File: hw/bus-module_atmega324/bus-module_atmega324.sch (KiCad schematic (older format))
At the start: 35 parts, among them J1 CONN_10X2, J2 CONN_10X2, J3 CONN-ISP-6, J5 CONN_1, J6 CONN_1, J7 CONN_1, J8 CONN_1, U1 ATMEGA324-TQFP44, U2 7,3728MHz, U3 25LCXXX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

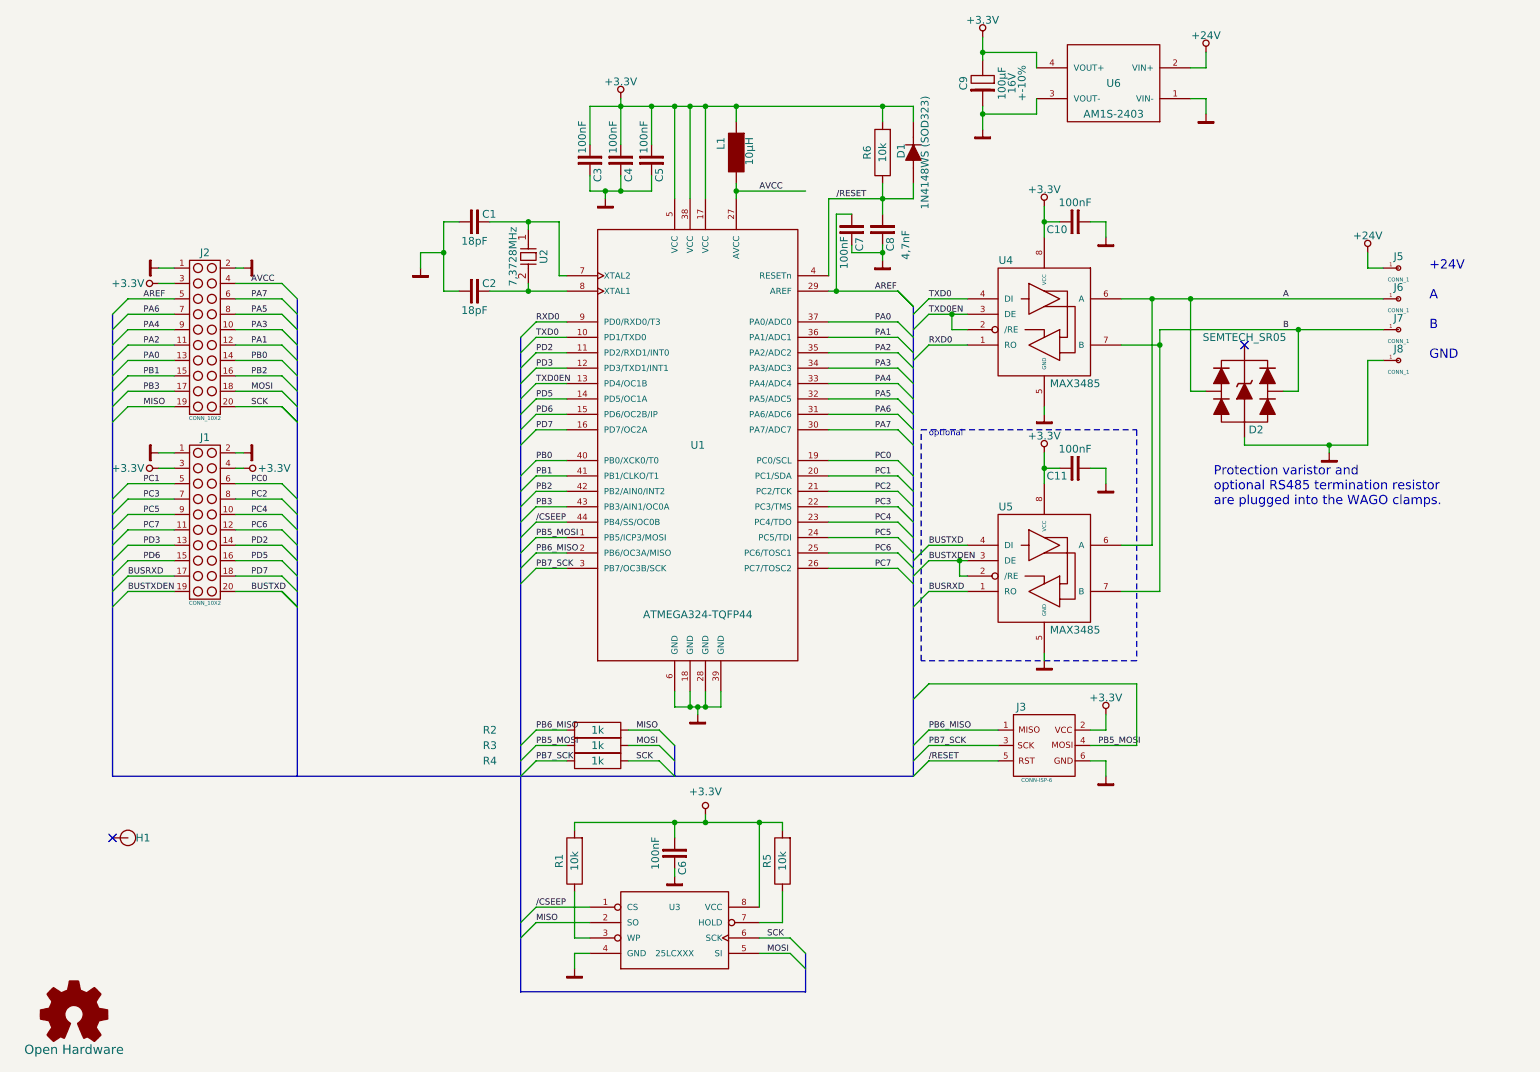
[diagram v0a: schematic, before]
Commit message: Start of development of Rev. B: - integrated fuse for 24V supply. - new footprint SOT143 for TVS-Diode. - replaced TVS-Diode footprint by SOT143. - added revision text on copper layer.
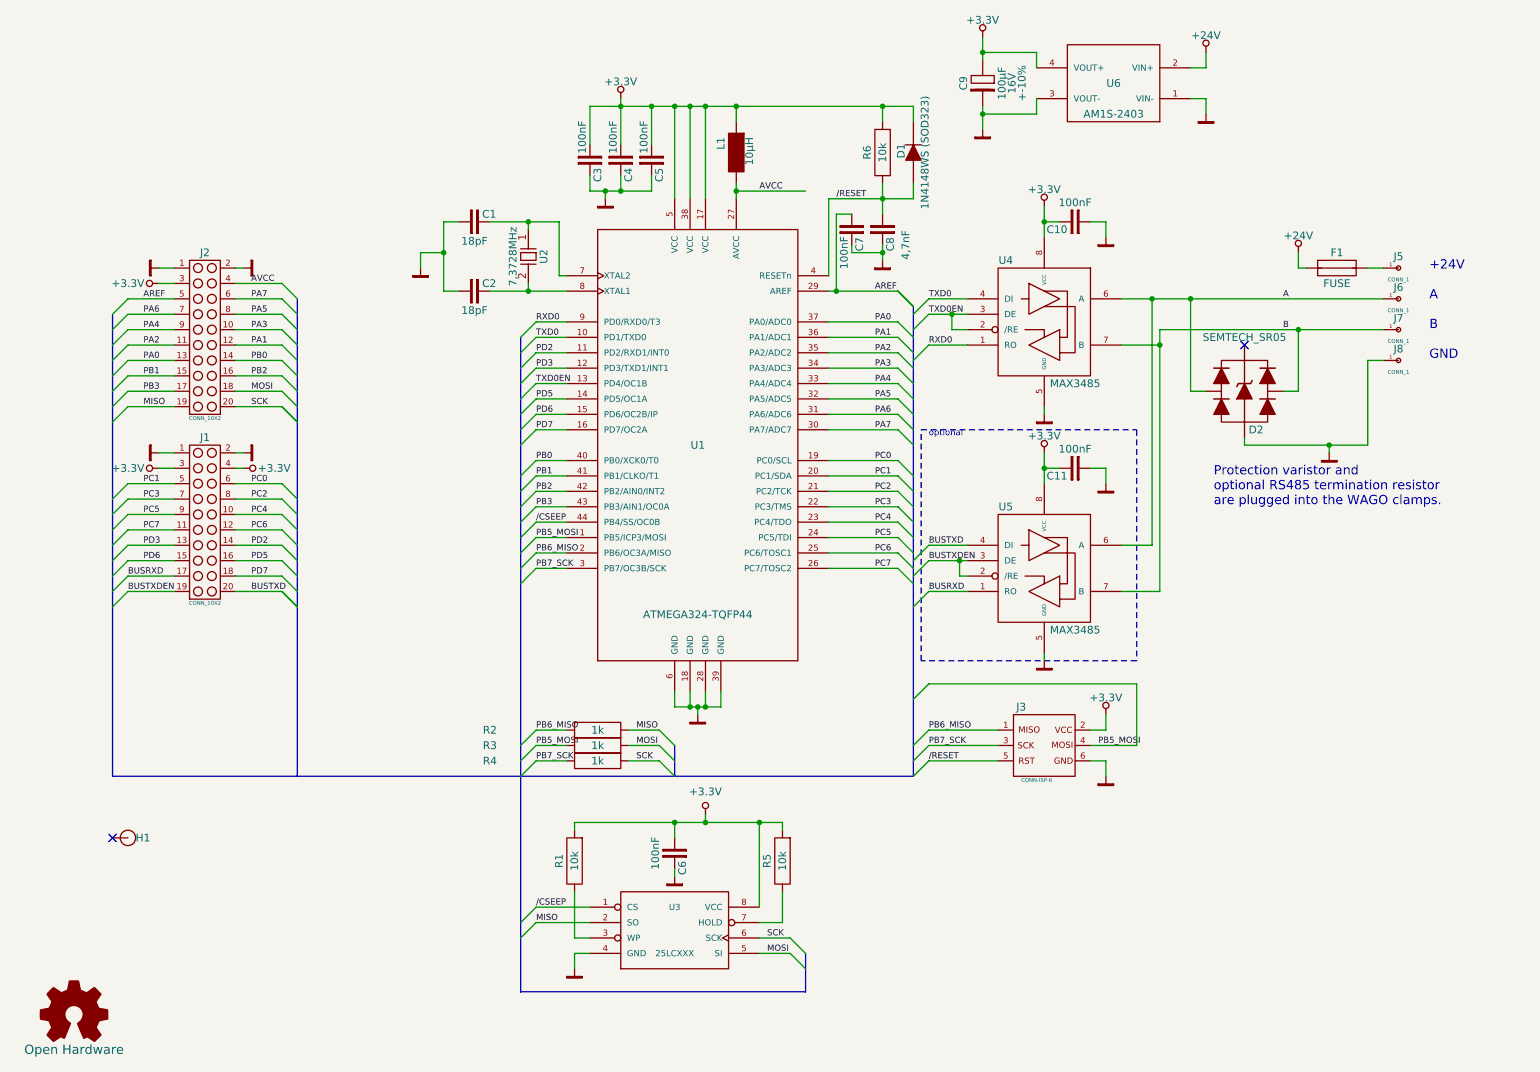
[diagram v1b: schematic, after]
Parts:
- added F1: FUSE, Resistor:R_1812, symbol FUSE
- D2: footprint Housings_SOT:SOT143R_Diode_Reverse -> Diode_SMD:SOT143
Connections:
- net +24V: now also F1.1; no longer J5.1
- new net: F1.2, J5.1
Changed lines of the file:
@@
 EESchema Schematic File Version 2
-LIBS:bus-module_atmega324-rescue
-LIBS:analog_devices
 LIBS:connectors
-LIBS:display
-LIBS:encoder
-LIBS:ftdi
 LIBS:ics_controller_atmel
 LIBS:ics_misc
-LIBS:ics_opamp
-LIBS:ics_opto
 LIBS:ics_peripheral
 LIBS:ics_regulator
 LIBS:logo
 LIBS:power
-LIBS:relays
-LIBS:sensors
 LIBS:standard
-LIBS:transformer
-LIBS:transistors
+LIBS:diodes
 LIBS:bus-module_atmega324-cache
 EELAYER 25 0
@@
 L +24V #PWR04
 U 1 1 559D77F1
-P 9700 2400
-F 0 "#PWR04" H 9700 2600 50  0001 C CNN
-F 1 "+24V" H 9700 2510 50  0000 C CNN
-F 2 "" H 9700 2400 60  0000 C CNN
-F 3 "" H 9700 2400 60  0000 C CNN
-	1    9700 2400
+P 9250 2400
+F 0 "#PWR04" H 9250 2600 50  0001 C CNN
+F 1 "+24V" H 9250 2510 50  0000 C CNN
+F 2 "" H 9250 2400 60  0000 C CNN
+F 3 "" H 9250 2400 60  0000 C CNN
+	1    9250 2400
 	1    0    0    -1
 $EndComp
@@
 	4300 5700 4500 5700
 Wire Bus Line
-	5200 5600 5200 5800
+	5200 5800 5200 5600
 Text Label 4300 6650 0    40   ~ 0
 /CSEEP
@@
 	5900 6750 5750 6750
 Wire Wire Line
-	5900 6150 5900 6100
-Wire Wire Line
-	5900 6100 4550 6100
+	5900 6100 5900 6150
+Wire Wire Line
+	4550 6100 5900 6100
 Wire Wire Line
 	4550 6100 4550 6150
@@
 $EndComp
 Wire Wire Line
-	9700 2400 9700 2500
+	9250 2400 9250 2500
 Wire Wire Line
 	9800 3100 9700 3100
@@
 F 0 "D2" H 8975 3050 50  0000 C CNN
 F 1 "SEMTECH_SR05" H 8900 3650 50  0000 C CNN
-F 2 "Housings_SOT:SOT143R_Diode_Reverse" H 8900 3300 60  0001 C CNN
+F 2 "Diode_SMD:SOT143" H 8900 3300 60  0001 C CNN
 F 3 "" H 8900 3300 60  0000 C CNN
 	1    8900 3300
 	1    0    0    -1
 $EndComp
-Wire Wire Line
-	9700 2500 9800 2500
 Wire Wire Line
 	9450 3650 9450 3700
@@
 	1    0    0    -1
 $EndComp
+$Comp
+L FUSE F1
+U 1 1 566474AD
+P 9500 2500
+F 0 "F1" H 9500 2600 50  0000 C CNN
+F 1 "FUSE" H 9500 2400 50  0000 C CNN
+F 2 "Resistor:R_1812" H 9500 2500 60  0001 C CNN
+F 3 "" H 9500 2500 60  0000 C CNN
+	1    9500 2500
+	1    0    0    -1
+$EndComp
+Wire Wire Line
+	9250 2500 9300 2500
+Wire Wire Line
+	9700 2500 9800 2500
 $EndSCHEMATC

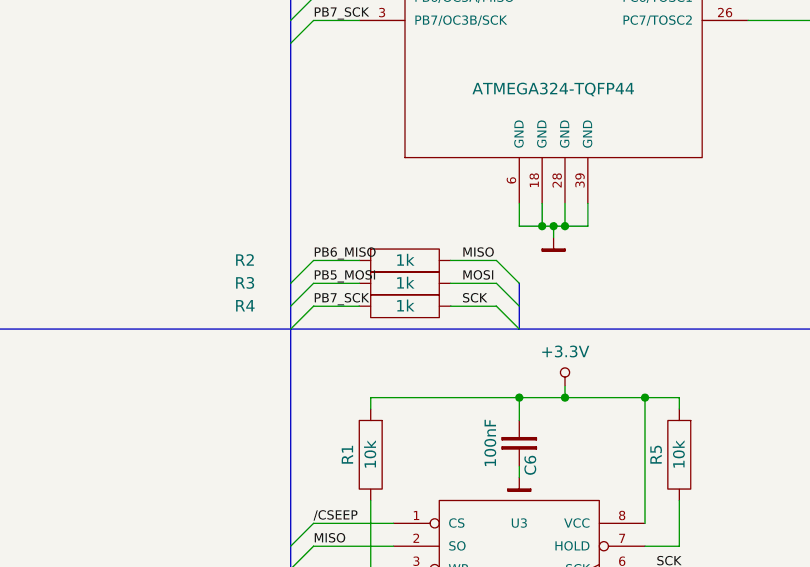
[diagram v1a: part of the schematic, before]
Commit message: SPI resistors changed from 1k to 100
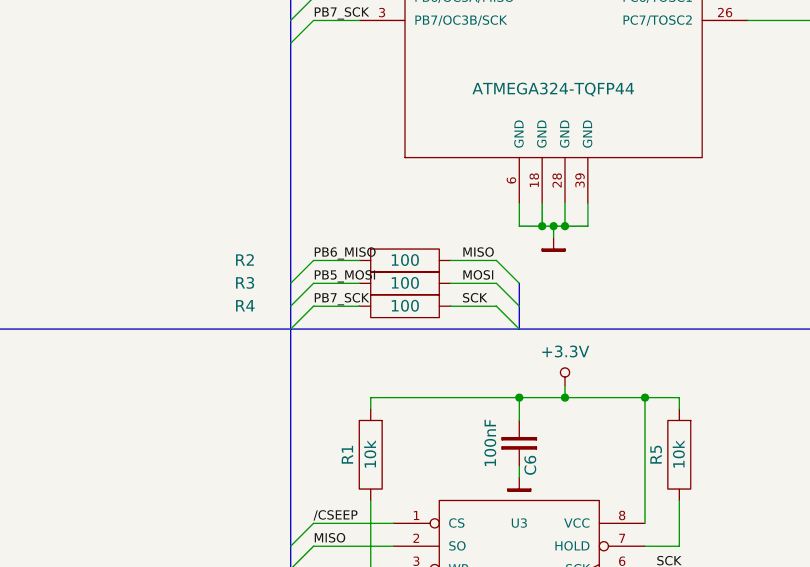
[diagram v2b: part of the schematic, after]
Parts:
- R2, R3, R4: value 1k -> 100
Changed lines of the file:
@@
 LIBS:diodes
 LIBS:bus-module_atmega324-cache
-EELAYER 25 0
+EELAYER 26 0
 EELAYER END
 $Descr A4 11693 8268
@@
 Sheet 1 1
 Title "bus-module_atmega324"
-Date "2015-10-19"
+Date "2017-02-10"
 Rev "1"
 Comp "KoeWiBa"
@@
 P 4700 5700
 F 0 "R4" H 4000 5700 50  0000 C CNN
-F 1 "1k" H 4700 5700 50  0000 C CNN
+F 1 "100" H 4700 5700 50  0000 C CNN
 F 2 "Housings_SOIC:SM0805" H 4700 5700 60  0001 C CNN
 F 3 "" H 4700 5700 60  0000 C CNN
@@
 P 4700 5600
 F 0 "R3" H 4000 5600 50  0000 C CNN
-F 1 "1k" H 4700 5600 50  0000 C CNN
+F 1 "100" H 4700 5600 50  0000 C CNN
 F 2 "Housings_SOIC:SM0805" H 4700 5600 60  0001 C CNN
 F 3 "" H 4700 5600 60  0000 C CNN
@@
 P 4700 5500
 F 0 "R2" H 4000 5500 50  0000 C CNN
-F 1 "1k" H 4700 5500 50  0000 C CNN
+F 1 "100" H 4700 5500 50  0000 C CNN
 F 2 "Housings_SOIC:SM0805" H 4700 5500 60  0001 C CNN
 F 3 "" H 4700 5500 60  0000 C CNN
